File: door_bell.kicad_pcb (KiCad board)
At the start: 4 copper layers, 68.6 x 68.6 mm, 75 parts, among them J1 8-10V AC/DC, J2 Speaker, J3 SWITCH1, J4 Door panel, J5 UART, J6 JTAG, J7 BOOT, J8 MicroSD, K1 HJR 1-2C, Q1 BC338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

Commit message: Start routing power rails
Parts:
- removed U6: ESP32-WROVER-B, RF_Module_espena:ESP32-WROVER-B
- D4, D5, D8: moved to B.Cu
- moved C1 2.39 mm to (153.2, 79.7)
- moved D2 0.74 mm to (142.0, 82.8)
- moved R6 0.73 mm to (123.2, 62.8)
- moved C2 0.41 mm to (127.0, 71.1)
- moved R16 0.25 mm to (135.3, 99.2)
- moved R15 0.13 mm to (133.1, 99.2)
- moved J5 0.09 mm to (151.8, 91.1)
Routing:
- net GND: track 0.00 -> 505.2 mm, vias 0 -> 43
- net Net-(J1-Pin_2): track 0.00 -> 28.6 mm
- net Net-(D1-Pad4): track 0.00 -> 15.6 mm, vias 0 -> 1
- net +5V: track 0.00 -> 7.15 mm
- net Net-(J1-Pin_1): track 0.00 -> 6.35 mm, vias 0 -> 1
- net Net-(D4-A2): track 0.00 -> 6.19 mm, vias 0 -> 1
- net Net-(D5-A2): track 0.00 -> 5.78 mm, vias 0 -> 1
- net Net-(D8-A2): track 0.00 -> 4.64 mm, vias 0 -> 1
- net Net-(D2-A): track 0.00 -> 4.26 mm
- net +3V3: track 0.00 -> 2.86 mm
- net Net-(D9-A2): track 0.00 -> 1.37 mm
- net Net-(D11-A2): track 0.00 -> 1.37 mm
- net Net-(D10-A2): track 0.00 -> 1.35 mm

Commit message: Rip-up and retry ...
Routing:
- net GND: track 505.2 -> 0.00 mm, vias 43 -> 0
- net Net-(J1-Pin_2): track 28.6 -> 0.00 mm
- net Net-(D1-Pad4): track 15.6 -> 0.00 mm, vias 1 -> 0
- net +5V: track 7.15 -> 0.00 mm
- net Net-(J1-Pin_1): track 6.35 -> 0.00 mm, vias 1 -> 0
- net Net-(D4-A2): track 6.19 -> 0.00 mm, vias 1 -> 0
- net Net-(D5-A2): track 5.78 -> 0.00 mm, vias 1 -> 0
- net Net-(D8-A2): track 4.64 -> 0.00 mm, vias 1 -> 0
- net Net-(D2-A): track 4.26 -> 0.00 mm
- net +3V3: track 2.86 -> 0.00 mm
- net Net-(D9-A2): track 1.37 -> 0.00 mm
- net Net-(D11-A2): track 1.37 -> 0.00 mm
- net Net-(D10-A2): track 1.35 -> 0.00 mm

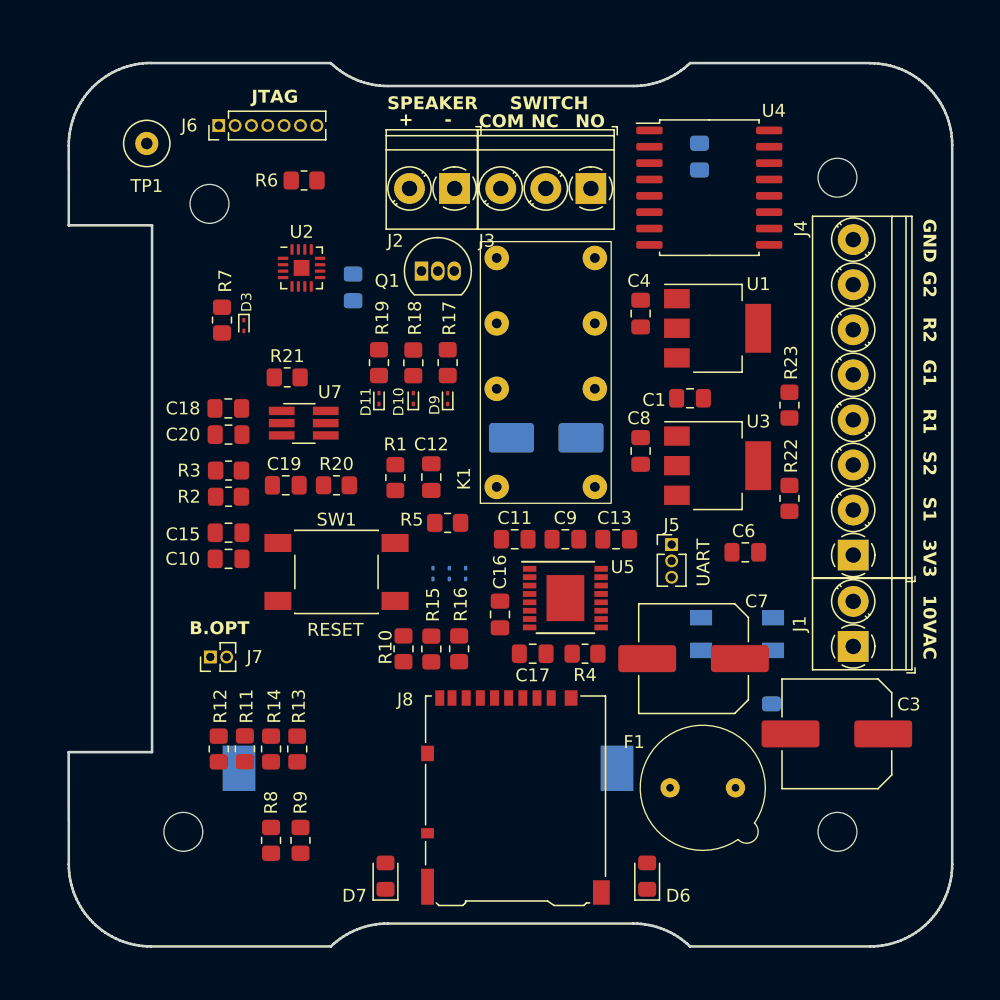
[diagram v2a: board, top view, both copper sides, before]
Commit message: GND plane routing
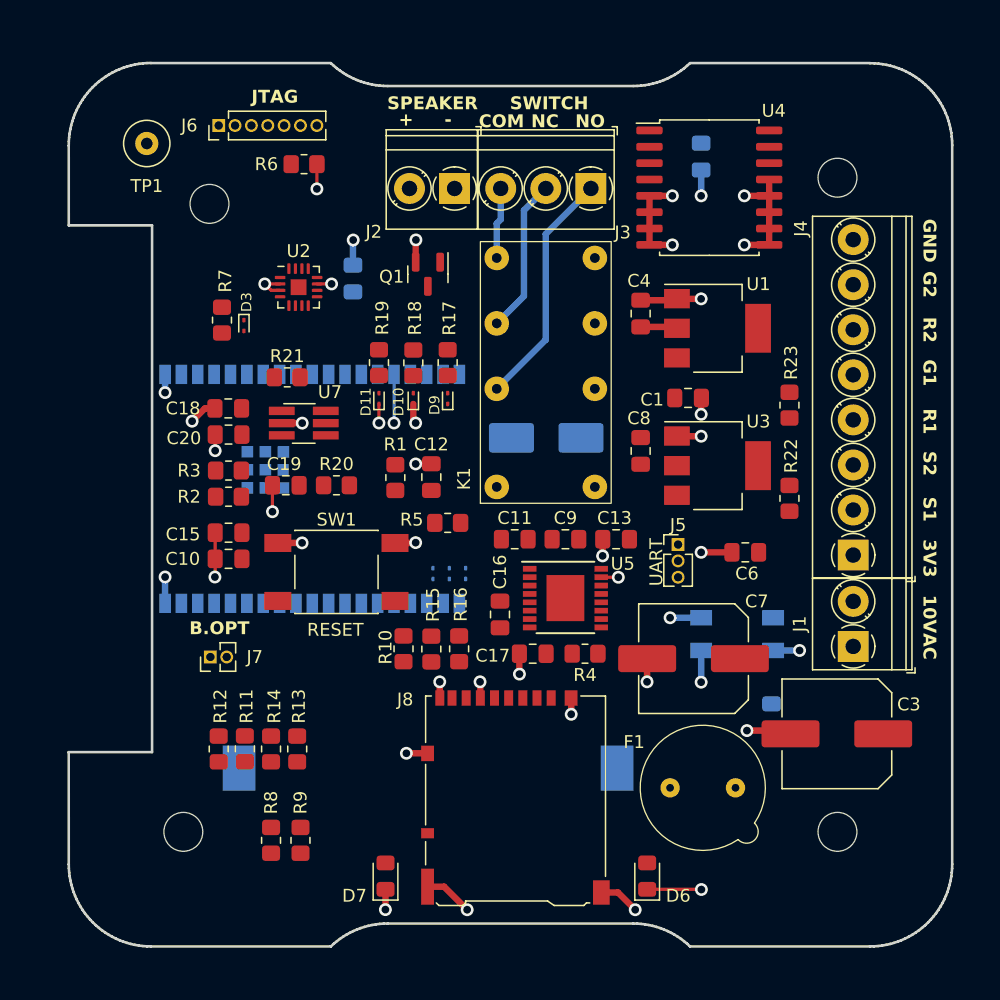
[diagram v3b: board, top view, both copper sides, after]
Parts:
- added U6: ESP32-WROVER-B, RF_Module_espena:ESP32-WROVER-B, B.Cu at (112.4, 77.9)
- Q1: value BC338 -> BC847; footprint Package_TO_SOT_THT:TO-92_Inline -> Package_TO_SOT_SMD:SOT-23
- moved U2 1.51 mm to (122.8, 71.1)
- moved R6 1.26 mm to (123.2, 61.5)
- moved C2 0.69 mm to (127.0, 70.4), turned to 90 degrees
- moved Q1 0.55 mm to (132.8, 70.1), turned to -90 degrees
- moved J5 0.50 mm to (152.3, 91.1)
- moved C1 0.15 mm to (153.0, 79.7)
- moved C14 0.13 mm to (154.1, 61.0)
- turned C6 to 180 degrees
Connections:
- C14 pad 1: +3V3 -> GND
- C14 pad 2: GND -> +3V3
- K1 pad 13: Net-(J3-Pin_3) -> Net-(J3-Pin_1)
- K1 pad 9: Net-(J3-Pin_1) -> Net-(J3-Pin_3)
- Q1 pad 1: Net-(D2-A) -> Net-(Q1-B)
- Q1 pad 2: Net-(Q1-B) -> GND
- Q1 pad 3: GND -> Net-(D2-A)
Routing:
- net GND: track 0.00 -> 420.3 mm, vias 0 -> 41
- net Net-(J1-Pin_2): track 0.00 -> 29.8 mm
- net Net-(J3-Pin_1): track 0.00 -> 18.6 mm
- net Net-(D1-Pad4): track 0.00 -> 15.6 mm, vias 0 -> 1
- net Net-(J3-Pin_2): track 0.00 -> 12.1 mm
- net Net-(J1-Pin_1): track 0.00 -> 6.35 mm, vias 0 -> 1
- net Net-(J3-Pin_3): track 0.00 -> 5.54 mm
- net +5V: track 0.00 -> 2.86 mm

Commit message: Initial routing of power rails and some signals
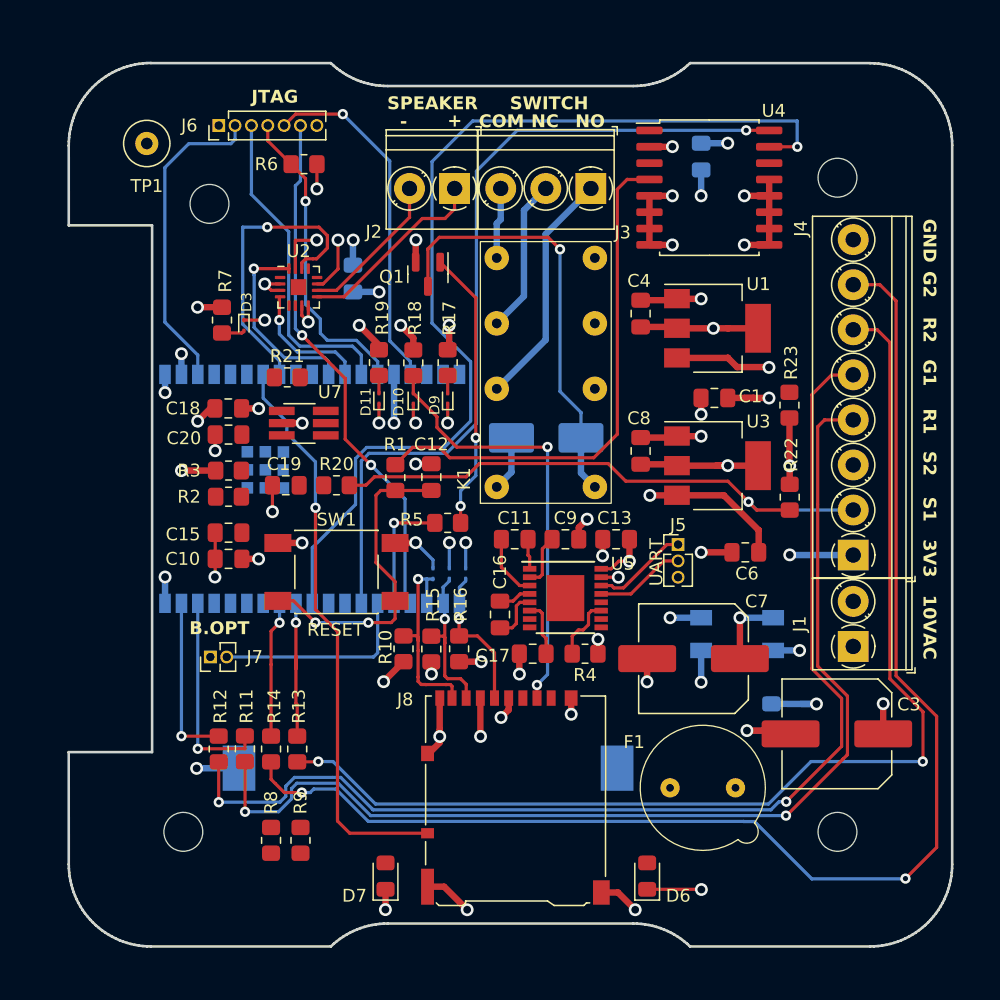
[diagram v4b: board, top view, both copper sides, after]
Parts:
- moved C1 2.05 mm to (155.1, 79.7), turned to 180 degrees
- moved R22 0.10 mm to (160.9, 87.4)
- turned C14 to 90 degrees
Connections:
- U2 pad 10: Net-(J2-Pin_1) -> Net-(J2-Pin_2)
- U2 pad 9: Net-(J2-Pin_2) -> Net-(J2-Pin_1)
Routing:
- net +3V3: track 0.00 -> 274.0 mm, vias 0 -> 20
- net /S2_GREEN: track 0.00 -> 105.3 mm, vias 0 -> 2
- net +5V: track 2.86 -> 96.2 mm, vias 0 -> 4
- net /S2_RED: track 0.00 -> 88.2 mm, vias 0 -> 2
- net /S1_GREEN: track 0.00 -> 88.0 mm, vias 0 -> 2
- net /S1_RED: track 0.00 -> 84.5 mm, vias 0 -> 2
- net /SDA: track 0.00 -> 78.0 mm, vias 0 -> 1
- net +VDC: track 0.00 -> 70.8 mm, vias 0 -> 5
- net /SCL: track 0.00 -> 64.9 mm, vias 0 -> 1
- net GND: track 420.3 -> 472.2 mm, vias 41 -> 46
- net Net-(D3-A2): track 0.00 -> 46.2 mm, vias 0 -> 1
- net /~{S1_INPUT}: track 0.00 -> 44.8 mm, vias 0 -> 1
- net Net-(J6-Pin_6): track 0.00 -> 41.0 mm, vias 0 -> 2
- net Net-(U4-~{RST}): track 0.00 -> 40.7 mm
- net Net-(D10-A2): track 0.00 -> 33.8 mm, vias 0 -> 2
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
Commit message: Done routing
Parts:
- J1, J2: footprint TerminalBlock_Phoenix:TerminalBlock_Phoenix_PT-1,5-2-3.5-H_1x02_P3.50mm_Horizontal -> TerminalBlock_Phoenix_espena:TerminalBlock_Phoenix_PT-1,5-2-3.5-H_1x02_P3.50mm_Horizontal_stackable
- J3: footprint TerminalBlock_Phoenix:TerminalBlock_Phoenix_PT-1,5-3-3.5-H_1x03_P3.50mm_Horizontal -> TerminalBlock_Phoenix_espena:TerminalBlock_Phoenix_PT-1,5-3-3.5-H_1x03_P3.50mm_Horizontal_stackable
- J4: footprint TerminalBlock_Phoenix:TerminalBlock_Phoenix_PT-1,5-8-3.5-H_1x08_P3.50mm_Horizontal -> TerminalBlock_Phoenix_espena:TerminalBlock_Phoenix_PT-1,5-8-3.5-H_1x08_P3.50mm_Horizontal_stackable
- moved BT1 0.06 mm to (132.8, 108.5)
- moved J3 0.06 mm to (145.4, 63.4)
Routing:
- net /~{S2_INPUT}: track 0.00 -> 68.7 mm, vias 0 -> 3
- net Net-(U6-SENSOR_VP): track 0.00 -> 63.1 mm, vias 0 -> 1
- net Net-(U5-T1IN): track 4.93 -> 61.8 mm, vias 0 -> 1
- net Net-(U5-R1OUT): track 0.00 -> 55.2 mm, vias 0 -> 1
- net Net-(BT1-+): track 0.00 -> 53.1 mm, vias 0 -> 1
- net Net-(D11-A2): track 1.37 -> 52.5 mm, vias 0 -> 3
- net Net-(U6-SENSOR_VN): track 0.00 -> 45.4 mm, vias 0 -> 3
- net Net-(D9-A2): track 1.37 -> 41.7 mm, vias 0 -> 3
- net Net-(D6-A): track 0.00 -> 34.3 mm, vias 0 -> 2
- net /DIN: track 0.00 -> 24.9 mm, vias 0 -> 1
- net Net-(U6-IO21): track 0.00 -> 23.6 mm, vias 0 -> 1
- net Net-(J6-Pin_2): track 24.6 -> 42.4 mm, vias 0 -> 1
- net Net-(C12-Pad2): track 24.6 -> 41.8 mm
- net Net-(C19-Pad1): track 0.00 -> 16.4 mm, vias 0 -> 2
- net +3V3: track 274.0 -> 287.8 mm, vias 20 -> 19
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- added copper zone on B.Cu, net (none)
- added copper zone on In2.Cu, net +3V3
- added copper zone on F.Cu, net GND
- added copper zone on In1.Cu, net GND
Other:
- outline, holes or cut-outs redrawn

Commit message: Prototype finished, sent to production
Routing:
- net GND: track 473.4 -> 543.6 mm, vias 46 -> 59
- added copper zone on B.Cu, net GND
- removed copper zone on B.Cu, net (none)

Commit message: Add STL file
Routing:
- net Net-(C12-Pad2): track 41.8 -> 42.9 mm
- net Net-(U5-C1-): track 4.96 -> 5.54 mm
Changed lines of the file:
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@@
   (segment (start 156.1175 59.9225) (end 156.12 59.92) (width 0.5) (layer "B.Cu") (net 5))
   (segment (start 113.6904 77.8764) (end 113.6904 76.2704) (width 0.5) (layer "B.Cu") (net 5))
+  (segment (start 141.51 93.625) (end 141.6558 93.4792) (width 0.25) (layer "F.Cu") (net 6))
+  (segment (start 141.6558 93.4792) (end 141.6558 92.7862) (width 0.25) (layer "F.Cu") (net 6))
   (segment (start 140.735 93.625) (end 141.51 93.625) (width 0.25) (layer "F.Cu") (net 6))
-  (segment (start 141.51 93.625) (end 141.6558 93.4792) (width 0.25) (layer "F.Cu") (net 6))
-  (segment (start 141.6558 92.202) (end 142.4725 91.3853) (width 0.25) (layer "F.Cu") (net 6))
-  (segment (start 142.4725 91.3853) (end 142.4725 90.678) (width 0.25) (layer "F.Cu") (net 6))
-  (segment (start 141.6558 93.4792) (end 141.6558 92.202) (width 0.25) (layer "F.Cu") (net 6))
+  (segment (start 142.4725 91.9695) (end 142.4725 90.678) (width 0.25) (layer "F.Cu") (net 6))
+  (segment (start 141.6558 92.7862) (end 142.4725 91.9695) (width 0.25) (layer "F.Cu") (net 6))
   (segment (start 140.6105 91.9295) (end 140.6105 90.678) (width 0.25) (layer "F.Cu") (net 7))
   (segment (start 140.735 92.975) (end 140.735 92.055) (width 0.25) (layer "F.Cu") (net 7))
   (segment (start 140.735 92.055) (end 140.61 91.93) (width 0.25) (layer "F.Cu") (net 7))
   (segment (start 140.61 91.93) (end 140.6105 91.9295) (width 0.25) (layer "F.Cu") (net 7))
-  (segment (start 140.735 94.275) (end 139.96 94.275) (width 0.25) (layer "F.Cu") (net 8))
-  (segment (start 139.96 94.275) (end 138.5355 92.8505) (width 0.25) (layer "F.Cu") (net 8))
-  (segment (start 138.5355 92.8505) (end 138.5355 90.678) (width 0.25) (layer "F.Cu") (net 8))
+  (segment (start 140.735 94.275) (end 138.979 94.275) (width 0.25) (layer "F.Cu") (net 8))
+  (segment (start 138.5355 93.8315) (end 138.5355 90.678) (width 0.25) (layer "F.Cu") (net 8))
+  (segment (start 138.979 94.275) (end 138.5355 93.8315) (width 0.25) (layer "F.Cu") (net 8))
+  (segment (start 124.09 96.15) (end 124.09 97.15) (width 0.25) (layer "F.Cu") (net 9))
   (segment (start 114.28 88.17) (end 115.074 87.376) (width 0.25) (layer "F.Cu") (net 9))
-  (segment (start 130.28 94.11) (end 130.28 95.468) (width 0.25) (layer "F.Cu") (net 9))
+  (segment (start 128.3705 86.8895) (end 130.302 86.8895) (width 0.25) (layer "F.Cu") (net 9))
   (segment (start 130.302 86.8895) (end 133.096 86.8895) (width 0.25) (layer "F.Cu") (net 9))
-  (segment (start 127.73 87.53) (end 127.73 91.56) (width 0.25) (layer "F.Cu") (net 9))
+  (segment (start 121.18 95.468) (end 123.408 95.468) (width 0.25) (layer "F.Cu") (net 9))
   (segment (start 115.074 87.376) (end 116.348 87.376) (width 0.25) (layer "F.Cu") (net 9))
-  (segment (start 122.408 95.468) (end 124.09 97.15) (width 0.25) (layer "F.Cu") (net 9))
-  (segment (start 121.18 95.468) (end 122.408 95.468) (width 0.25) (layer "F.Cu") (net 9))
+  (segment (start 127.73 87.53) (end 128.3705 86.8895) (width 0.25) (layer "F.Cu") (net 9))
+  (segment (start 130.28 95.468) (end 130.28 93.196) (width 0.25) (layer "F.Cu") (net 9))
+  (segment (start 130.28 93.196) (end 129.616 92.532) (width 0.25) (layer "F.Cu") (net 9))
+  (segment (start 128.702 92.532) (end 127.73 91.56) (width 0.25) (layer "F.Cu") (net 9))
   (segment (start 114.28 94.28) (end 114.28 88.17) (width 0.25) (layer "F.Cu") (net 9))
   (segment (start 115.468 95.468) (end 114.28 94.28) (width 0.25) (layer "F.Cu") (net 9))
-  (segment (start 128.3705 86.8895) (end 130.302 86.8895) (width 0.25) (layer "F.Cu") (net 9))
+  (segment (start 127.73 91.56) (end 127.73 87.53) (width 0.25) (layer "F.Cu") (net 9))
   (segment (start 130.28 96.85) (end 129.98 97.15) (width 0.25) (layer "F.Cu") (net 9))
   (segment (start 121.18 95.468) (end 115.468 95.468) (width 0.25) (layer "F.Cu") (net 9))
-  (segment (start 127.73 91.56) (end 130.28 94.11) (width 0.25) (layer "F.Cu") (net 9))
   (segment (start 130.28 95.468) (end 130.28 96.85) (width 0.25) (layer "F.Cu") (net 9))
-  (segment (start 127.73 87.53) (end 128.3705 86.8895) (width 0.25) (layer "F.Cu") (net 9))
+  (segment (start 129.616 92.532) (end 128.702 92.532) (width 0.25) (layer "F.Cu") (net 9))
   (segment (start 129.98 97.15) (end 128.2059 97.15) (width 0.25) (layer "F.Cu") (net 9))
+  (segment (start 123.408 95.468) (end 124.09 96.15) (width 0.25) (layer "F.Cu") (net 9))
   (via (at 128.2059 97.15) (size 0.8) (drill 0.4) (layers "F.Cu" "B.Cu") (net 9))
   (via (at 124.09 97.15) (size 0.8) (drill 0.4) (layers "F.Cu" "B.Cu") (net 9))

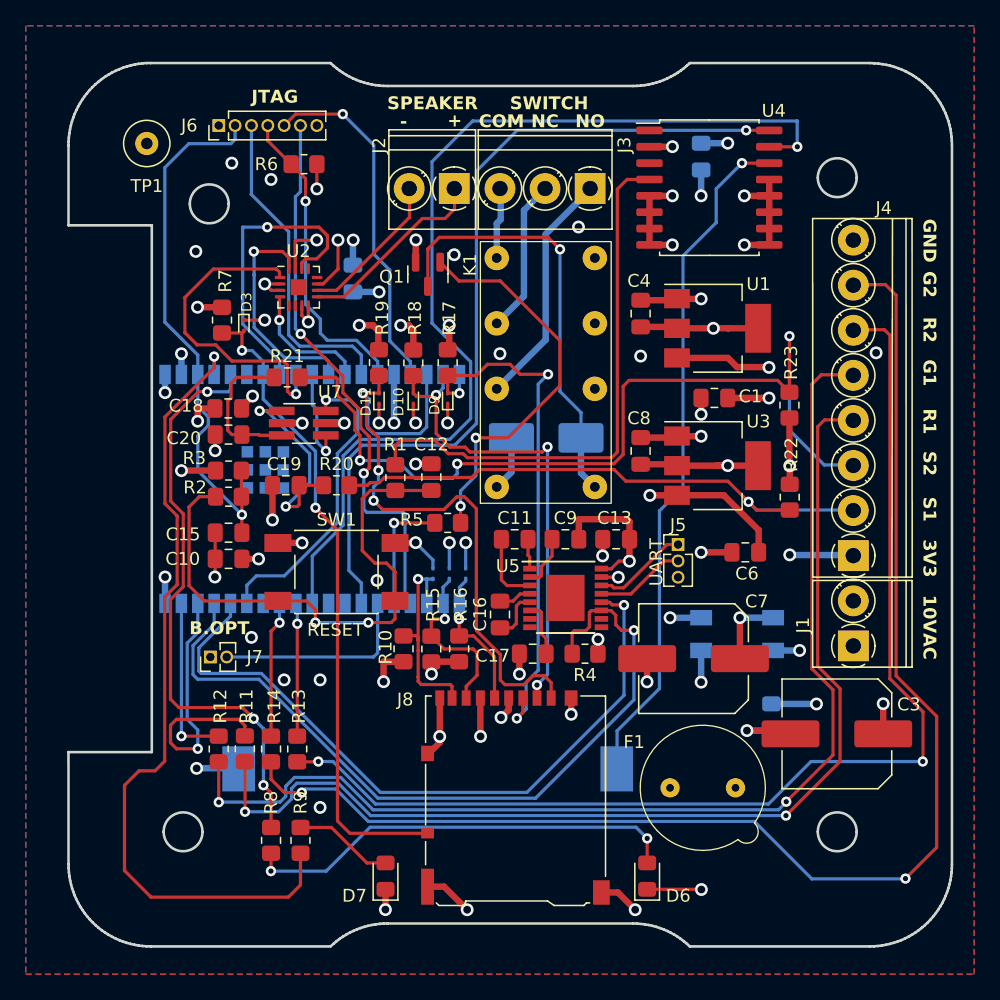
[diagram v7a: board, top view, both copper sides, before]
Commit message: Redraw, v.1.1 - fix errors
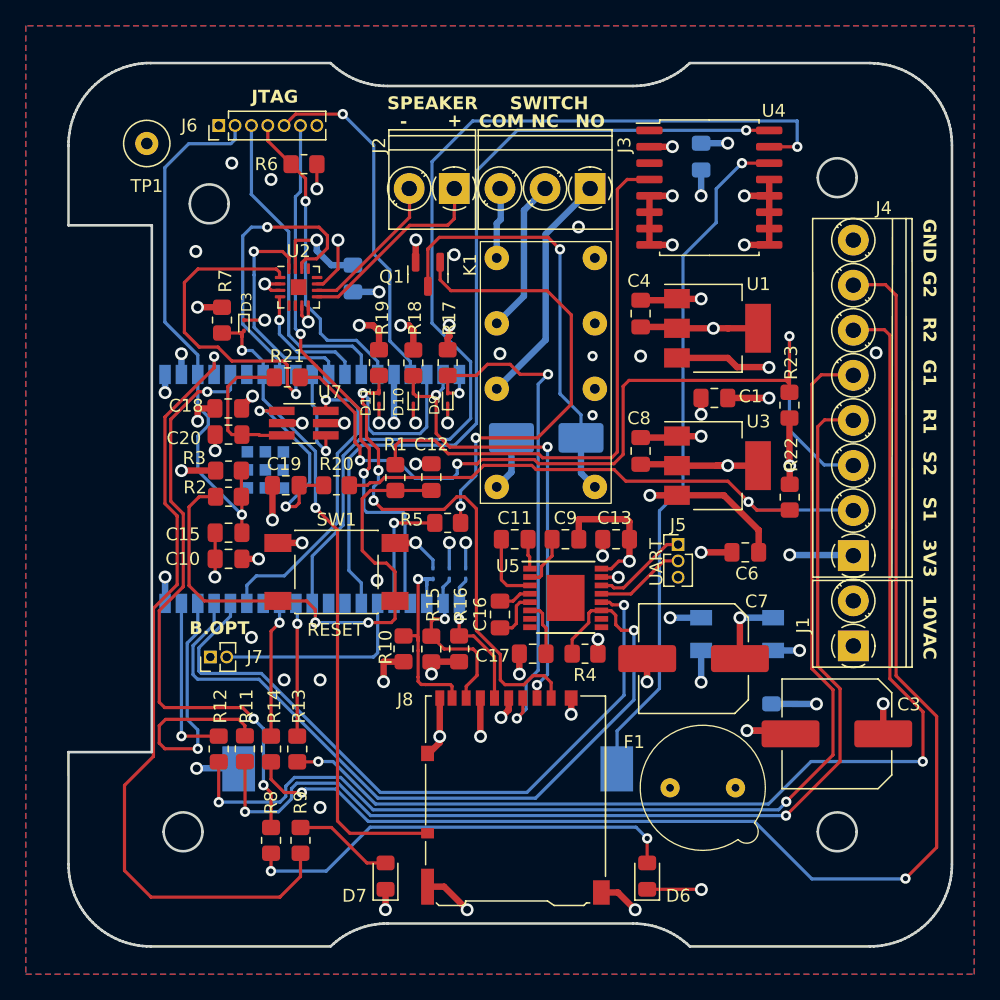
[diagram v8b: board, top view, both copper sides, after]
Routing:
- net Net-(Q1-B): track 30.6 -> 35.2 mm
- net GND: track 543.6 -> 545.8 mm, vias 59 -> 60
- net Net-(U6-IO22): track 22.6 -> 24.4 mm
- net Net-(U6-SENSOR_VN): track 45.4 -> 46.8 mm
- net Net-(U6-SENSOR_VP): track 63.1 -> 62.0 mm
- net Net-(D4-A2): track 16.1 -> 16.9 mm
- net Net-(D11-A2): track 52.5 -> 53.1 mm
- net Net-(U5-T1IN): track 61.8 -> 61.3 mm
